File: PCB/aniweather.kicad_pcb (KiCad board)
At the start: 2 copper layers, 55 x 75 mm, 36 parts, among them SW1 SW_DIP_x01, SW2 SW_Push, SW3 SW_Push, U5 TPS63001

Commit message: Really last rev
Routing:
- net GND: track 18.2 -> 17.1 mm, vias 50 -> 48
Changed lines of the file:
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@@
 			(plot_on_all_layers_selection 0x00000000_00000000)
 			(disableapertmacros no)
-			(usegerberextensions no)
-			(usegerberattributes yes)
-			(usegerberadvancedattributes yes)
-			(creategerberjobfile yes)
+			(usegerberextensions yes)
+			(usegerberattributes no)
+			(usegerberadvancedattributes no)
+			(creategerberjobfile no)
 			(dashed_line_dash_ratio 12.000000)
 			(dashed_line_gap_ratio 3.000000)
@@
 			(sketchdnponfab yes)
 			(crossoutdnponfab yes)
-			(subtractmaskfromsilk no)
+			(subtractmaskfromsilk yes)
 			(outputformat 1)
 			(mirror no)
-			(drillshape 1)
+			(drillshape 0)
 			(scaleselection 1)
-			(outputdirectory "")
+			(outputdirectory "production/gerbers/")
 		)
 	)
@@
 	)
 	(segment
+		(start 144.45 99.775)
+		(end 143.5 100.725)
+		(width 0.5)
+		(layer "F.Cu")
+		(net 6)
+	)
+	(segment
 		(start 147.75 93.175)
 		(end 147.75 91.175)
@@
 	)
 	(segment
-		(start 144.9 99.325)
-		(end 143.5 100.725)
-		(width 0.5)
-		(layer "F.Cu")
-		(net 6)
-	)
-	(segment
 		(start 147.25 90.675)
 		(end 147.25 89.375)
@@
 	)
 	(via
-		(at 144.9 99.325)
-		(size 0.6)
-		(drill 0.3)
+		(at 144.45 99.775)
+		(size 1)
+		(drill 0.6)
 		(layers "F.Cu" "B.Cu")
 		(net 6)
@@
 	)
 	(segment
+		(start 144.9 99.325)
+		(end 144.45 99.775)
+		(width 0.5)
+		(layer "B.Cu")
+		(net 6)
+	)
+	(segment
 		(start 146.54 97.685)
 		(end 146.54 95.565)
@@
 	)
 	(segment
-		(start 136.395 75.22)
-		(end 137.4 76.225)
+		(start 137.9 76.225)
+		(end 138.084 76.409)
 		(width 0.3)
 		(layer "F.Cu")
@@
 	)
 	(segment
-		(start 137.9 76.225)
-		(end 138.084 76.409)
+		(start 138.084 77.909)
+		(end 138.3 78.125)
 		(width 0.3)
 		(layer "F.Cu")
@@
 	)
 	(segment
-		(start 138.084 77.909)
-		(end 138.3 78.125)
+		(start 137.4 76.225)
+		(end 137.9 76.225)
 		(width 0.3)
 		(layer "F.Cu")
@@
 	)
 	(segment
-		(start 138.084 76.409)
-		(end 138.084 77.909)
+		(start 149.08 95.565)
+		(end 149.08 88.755)
+		(width 0.5)
+		(layer "F.Cu")
+		(net 10)
+	)
+	(segment
+		(start 149.08 88.755)
+		(end 146.65 86.325)
+		(width 0.5)
+		(layer "F.Cu")
+		(net 10)
+	)
+	(segment
+		(start 138.3 78.125)
+		(end 138.575 78.125)
 		(width 0.3)
 		(layer "F.Cu")
@@
 	)
 	(segment
-		(start 136.395 74.425)
-		(end 136.395 75.22)
+		(start 138.084 76.409)
+		(end 138.084 77.909)
 		(width 0.3)
 		(layer "F.Cu")
@@
 	)
 	(segment
-		(start 138.3 78.125)
-		(end 138.3 78.325)
+		(start 146.65 86.325)
+		(end 146.25 86.325)
 		(width 0.5)
 		(layer "F.Cu")
@@
 	)
 	(segment
-		(start 138.3 78.325)
-		(end 149.08 89.105)
-		(width 0.5)
+		(start 136.395 74.425)
+		(end 136.395 75.22)
+		(width 0.3)
+		(layer "F.Cu")
+		(net 10)
+	)
+	(segment
+		(start 136.395 75.22)
+		(end 137.4 76.225)
+		(width 0.3)
 		(layer "F.Cu")
 		(net 10)
 	)
 	(segment
-		(start 149.08 89.105)
-		(end 149.08 95.565)
+		(start 138.575 78.125)
+		(end 146.25 85.8)
 		(width 0.5)
 		(layer "F.Cu")
@@
 	)
 	(segment
-		(start 137.4 76.225)
-		(end 137.9 76.225)
-		(width 0.3)
+		(start 146.25 85.8)
+		(end 146.25 86.325)
+		(width 0.5)
 		(layer "F.Cu")
 		(net 10)
@@
 	)
 	(via
-		(at 150.7 136.925)
-		(size 0.6)
-		(drill 0.3)
-		(layers "F.Cu" "B.Cu")
-		(free yes)
-		(net 14)
-	)
-	(via
 		(at 130.225 119.4)
 		(size 1)
@@
 	)
 	(via
-		(at 120.15 118.775)
-		(size 0.6)
-		(drill 0.3)
-		(layers "F.Cu" "B.Cu")
-		(free yes)
-		(net 14)
-	)
-	(via
 		(at 150.15 68.7)
 		(size 1)
@@
 		(layer "B.Cu")
 		(net 14)
-	)
-	(segment
-		(start 120.15 118.775)
-		(end 120.15 117.625)
-		(width 0.75)
-		(layer "B.Cu")
-		(net 14)

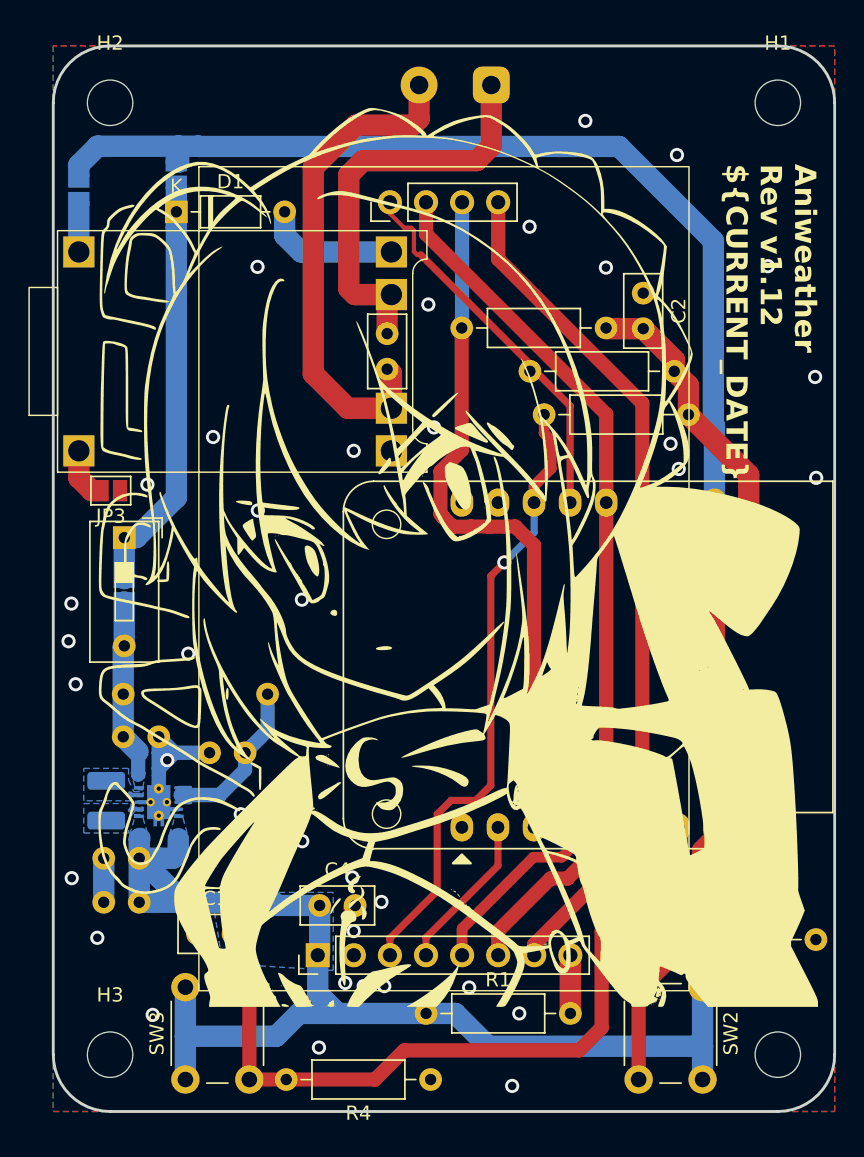
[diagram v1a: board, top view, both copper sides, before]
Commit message: Add diode to increase current capacity
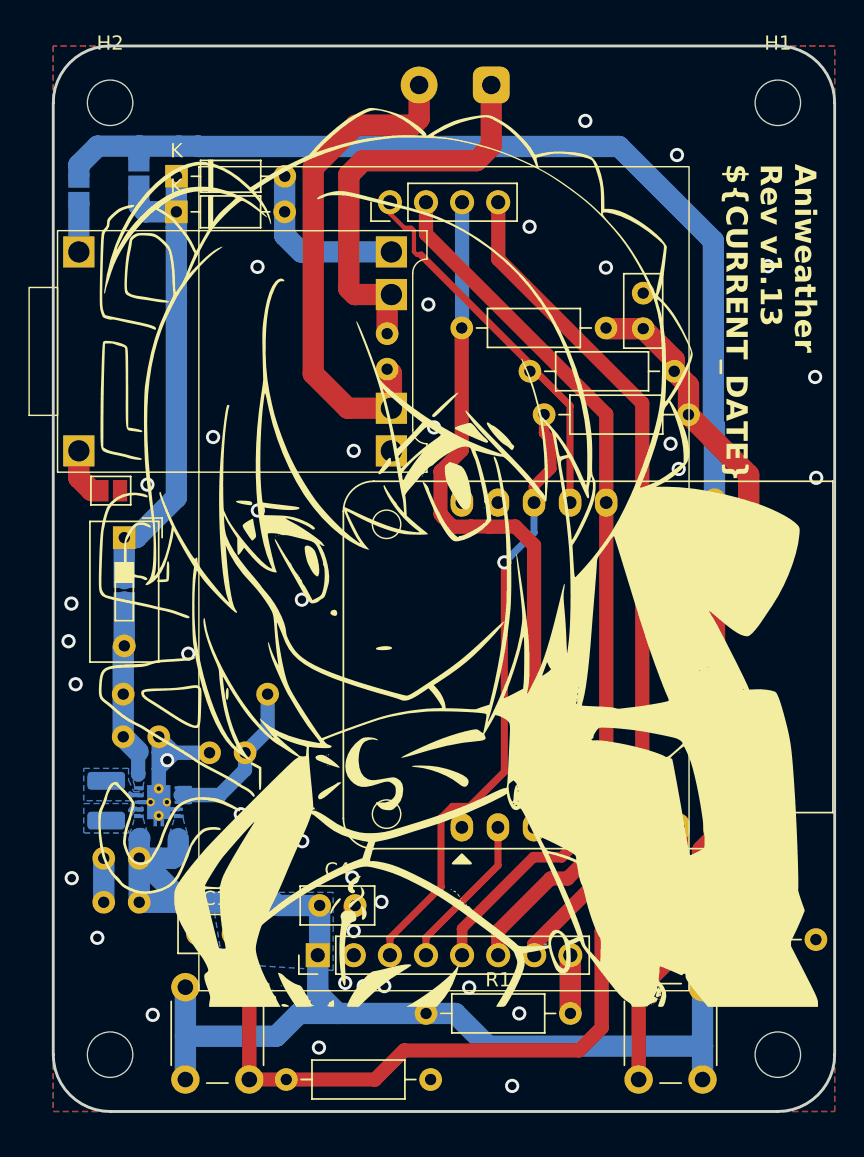
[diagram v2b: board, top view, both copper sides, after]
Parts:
- added D2: D, Diode_THT:D_DO-35_SOD27_P7.62mm_Horizontal, F.Cu at (121.4, 72.6)
- C3: moved to B.Cu
- moved JP4 2.62 mm to (118.7, 72.4)
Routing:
- net Net-(D1-K): track 31.6 -> 35.0 mm
- net Net-(D1-A): track 9.66 -> 12.2 mm
- net +3.3V: track 139.0 -> 138.4 mm
- net VBUS: track 68.4 -> 67.9 mm

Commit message: Readme and last rev
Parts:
- moved C3 2.68 mm to (138.9, 83.7)
- moved JP4 1.25 mm to (118.7, 73.7)
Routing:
- net +3.3V: track 138.4 -> 156.2 mm
- net Net-(BT1-+): track 29.2 -> 31.4 mm
- net Net-(BT1--): track 35.1 -> 36.9 mm
- net CS_LCD: track 43.7 -> 42.5 mm
- net Net-(D1-K): track 35.0 -> 34.0 mm
- net GND: track 17.1 -> 17.0 mm, vias 48 -> 50

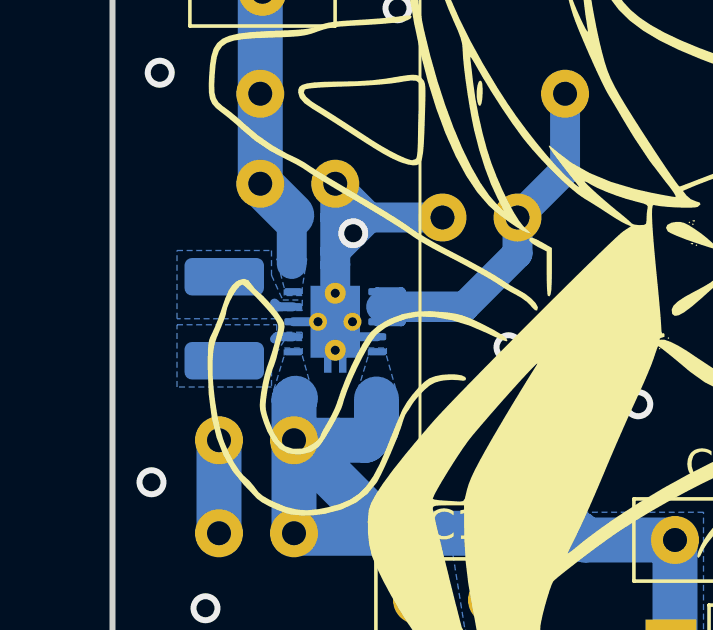
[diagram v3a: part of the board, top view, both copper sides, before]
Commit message: Improve inductor footprint
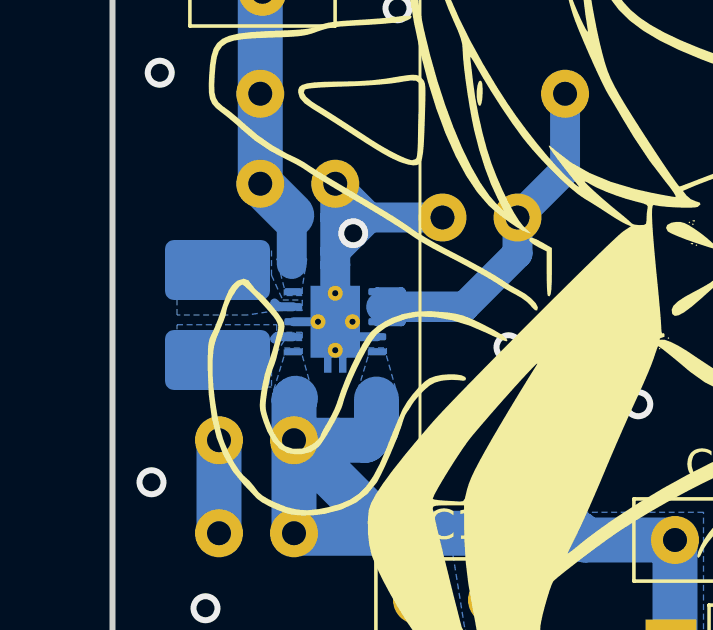
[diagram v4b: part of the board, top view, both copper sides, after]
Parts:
- L1: footprint Inductor_SMD:L_1210_3225Metric -> asylum:NR3015T2R2M
- moved L1 0.30 mm to (116.7, 116.4)

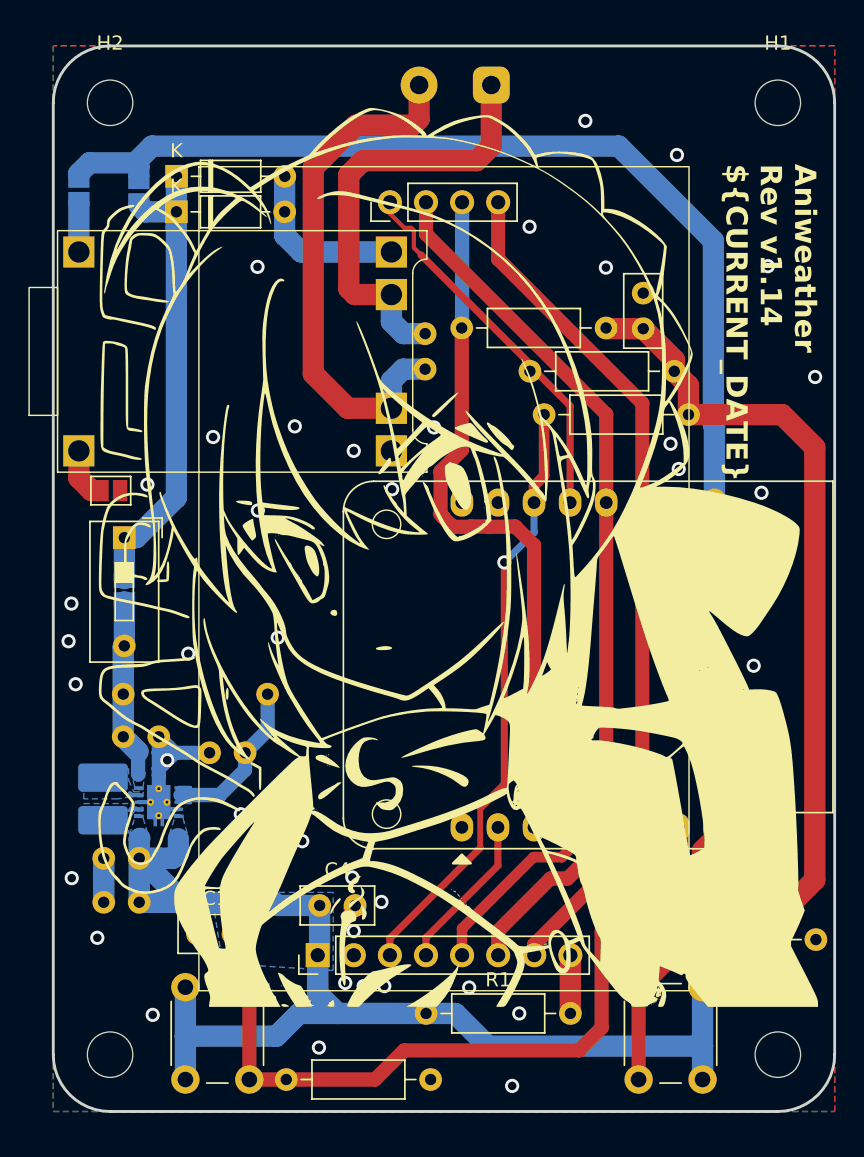
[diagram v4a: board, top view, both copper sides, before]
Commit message: Priority Power MUX
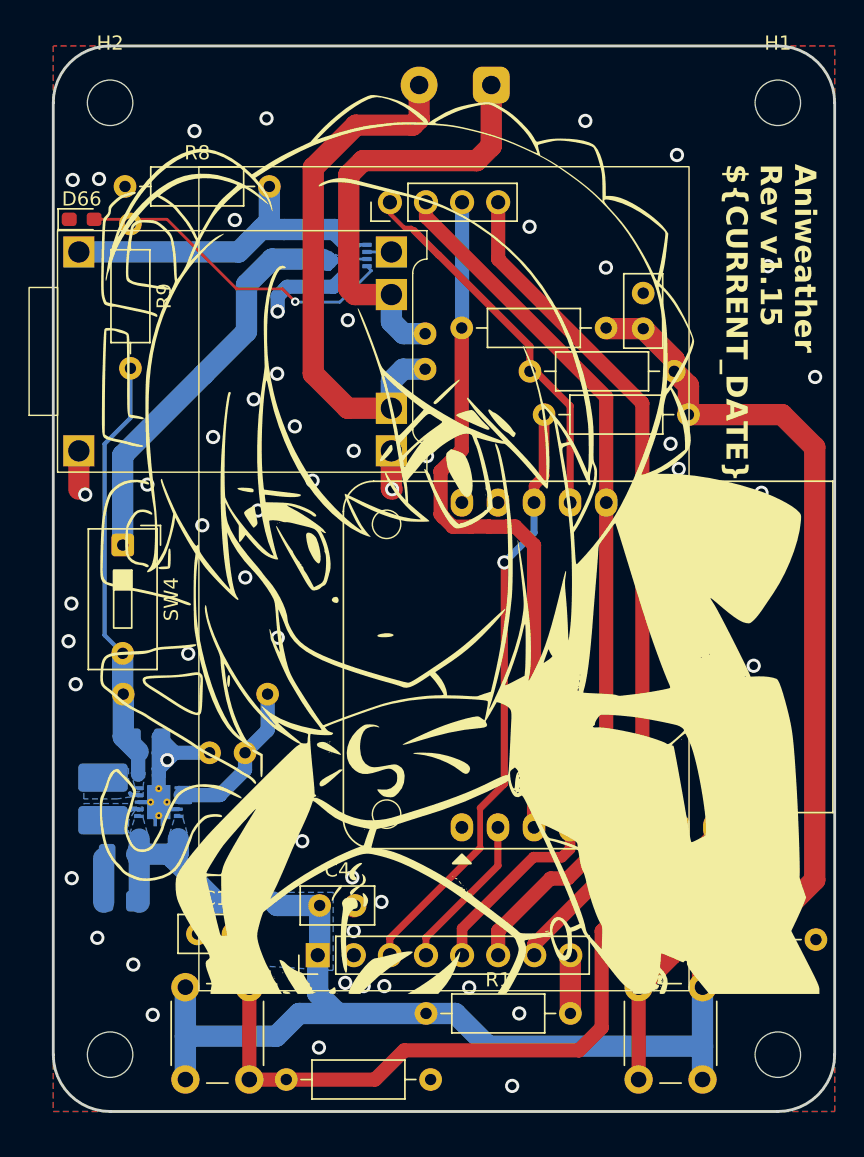
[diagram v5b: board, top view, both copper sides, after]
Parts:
- removed D1, D2: D, Diode_THT:D_DO-35_SOD27_P7.62mm_Horizontal
- removed JP1, JP2, JP3, JP4: Jumper_2_Open, Jumper:SolderJumper-2_P1.3mm_Open_Pad1.0x1.5mm
- removed SW1: SW_DIP_x01, Button_Switch_THT:SW_DIP_SPSTx01_Slide_9.78x4.72mm_W7.62mm_P2.54mm
- added D66: LED, LED_SMD:LED_0603_1608Metric_Pad1.05x0.95mm_HandSolder, F.Cu at (114.7, 75.6)
- added R8: 10k, Resistor_THT:R_Axial_DIN0207_L6.3mm_D2.5mm_P10.16mm_Horizontal, F.Cu at (117.8, 73.3)
- added R9: 470Ω, Resistor_THT:R_Axial_DIN0207_L6.3mm_D2.5mm_P10.16mm_Horizontal, F.Cu at (118.1, 76.0)
- added SW4: SW_DIP_x01, Button_Switch_THT:SW_DIP_SPSTx01_Slide_9.78x4.72mm_W7.62mm_P2.54mm, F.Cu at (117.6, 98.6)
- added U4: TPS2116DRL, Package_TO_SOT_SMD:SOT-583-8, B.Cu at (134.0, 78.2)
- C6, C7, C8: footprint Capacitor_THT:C_Disc_D5.0mm_W2.5mm_P2.50mm -> Capacitor_SMD:C_0805_2012Metric_Pad1.18x1.45mm_HandSolder
- R3, R4: value 100k -> 10k
- moved C6 1.70 mm to (119.3, 112.2)
- moved C8 1.38 mm to (117.4, 123.6)
- moved C7 1.25 mm to (117.5, 120.3)
- moved G1 0.92 mm to (140.4, 95.1)
- moved G2 0.92 mm to (140.4, 95.1)
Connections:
- net Net-(JP1-A) renamed +5V
- U2 pad 14: VBUS -> unconnected-(U2-VBUS-Pad14)
- U3 pad 2: Net-(D1-A) -> BOUT
- U3 pad 4: Net-(JP2-A) -> VIN+
- U3 pad 5: Net-(JP3-B) -> GND
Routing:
- net VBUS: track 67.7 -> 0.00 mm
- net Net-(SW4-Pad1): track 0.00 -> 34.6 mm
- net Net-(D1-K): track 34.0 -> 0.00 mm
- net VIN+: track 0.00 -> 28.7 mm
- net Net-(D66-A): track 0.00 -> 23.3 mm, vias 0 -> 1
- net +5V: track 12.6 -> 30.3 mm
- net Net-(D1-A): track 12.2 -> 0.00 mm
- net GND: track 17.0 -> 29.1 mm, vias 50 -> 63
- net +3.3V: track 156.2 -> 148.1 mm
- net Net-(JP3-B): track 3.57 -> 0.00 mm
- net Net-(JP2-A): track 3.45 -> 0.00 mm
- net BOUT: track 0.00 -> 1.72 mm
- added copper zone on B.Cu, net Net-(SW4-Pad1)

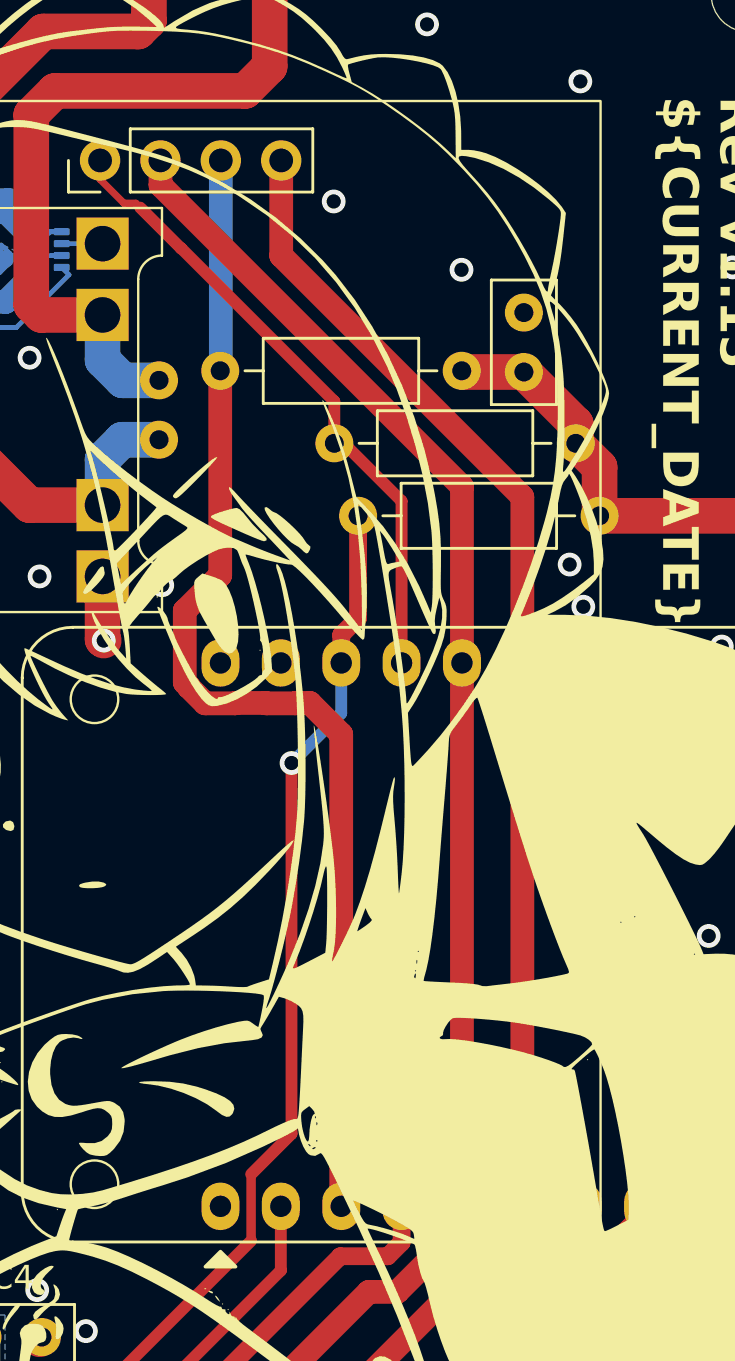
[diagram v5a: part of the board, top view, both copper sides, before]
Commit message: FIX MISO and MOSI order
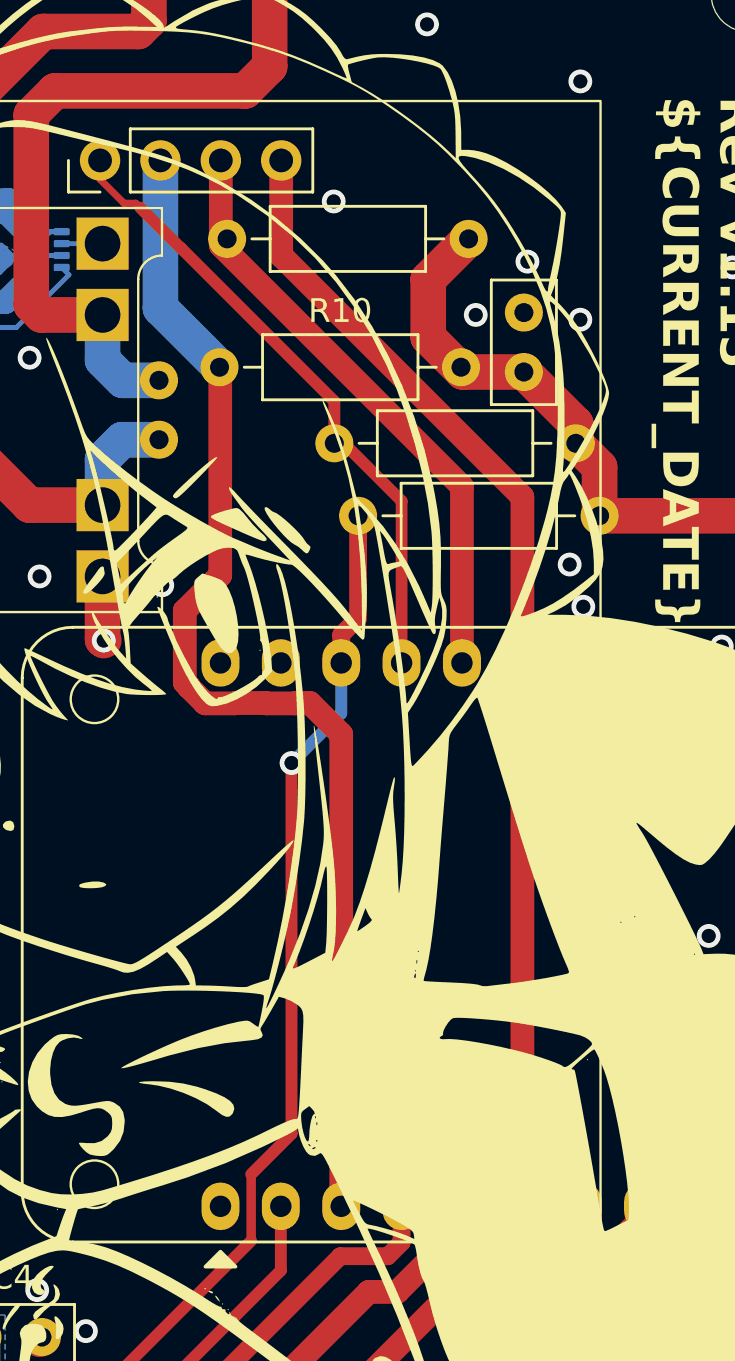
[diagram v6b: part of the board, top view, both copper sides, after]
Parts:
- added R10: 10k, Resistor_THT:R_Axial_DIN0207_L6.3mm_D2.5mm_P10.16mm_Horizontal, F.Cu at (141.4, 83.1)
- moved R7 5.56 mm to (141.7, 77.7)
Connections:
- U2 pad 2: MISO -> MOSI
- U2 pad 7: MOSI -> MISO
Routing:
- net MISO: track 50.0 -> 25.3 mm
- net +3.3V: track 148.1 -> 155.0 mm
- net MOSI: track 62.1 -> 68.8 mm
- net GND: vias 63 -> 65
